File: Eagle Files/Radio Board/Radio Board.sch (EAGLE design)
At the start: 15 parts, among them Y1 16 MHZ

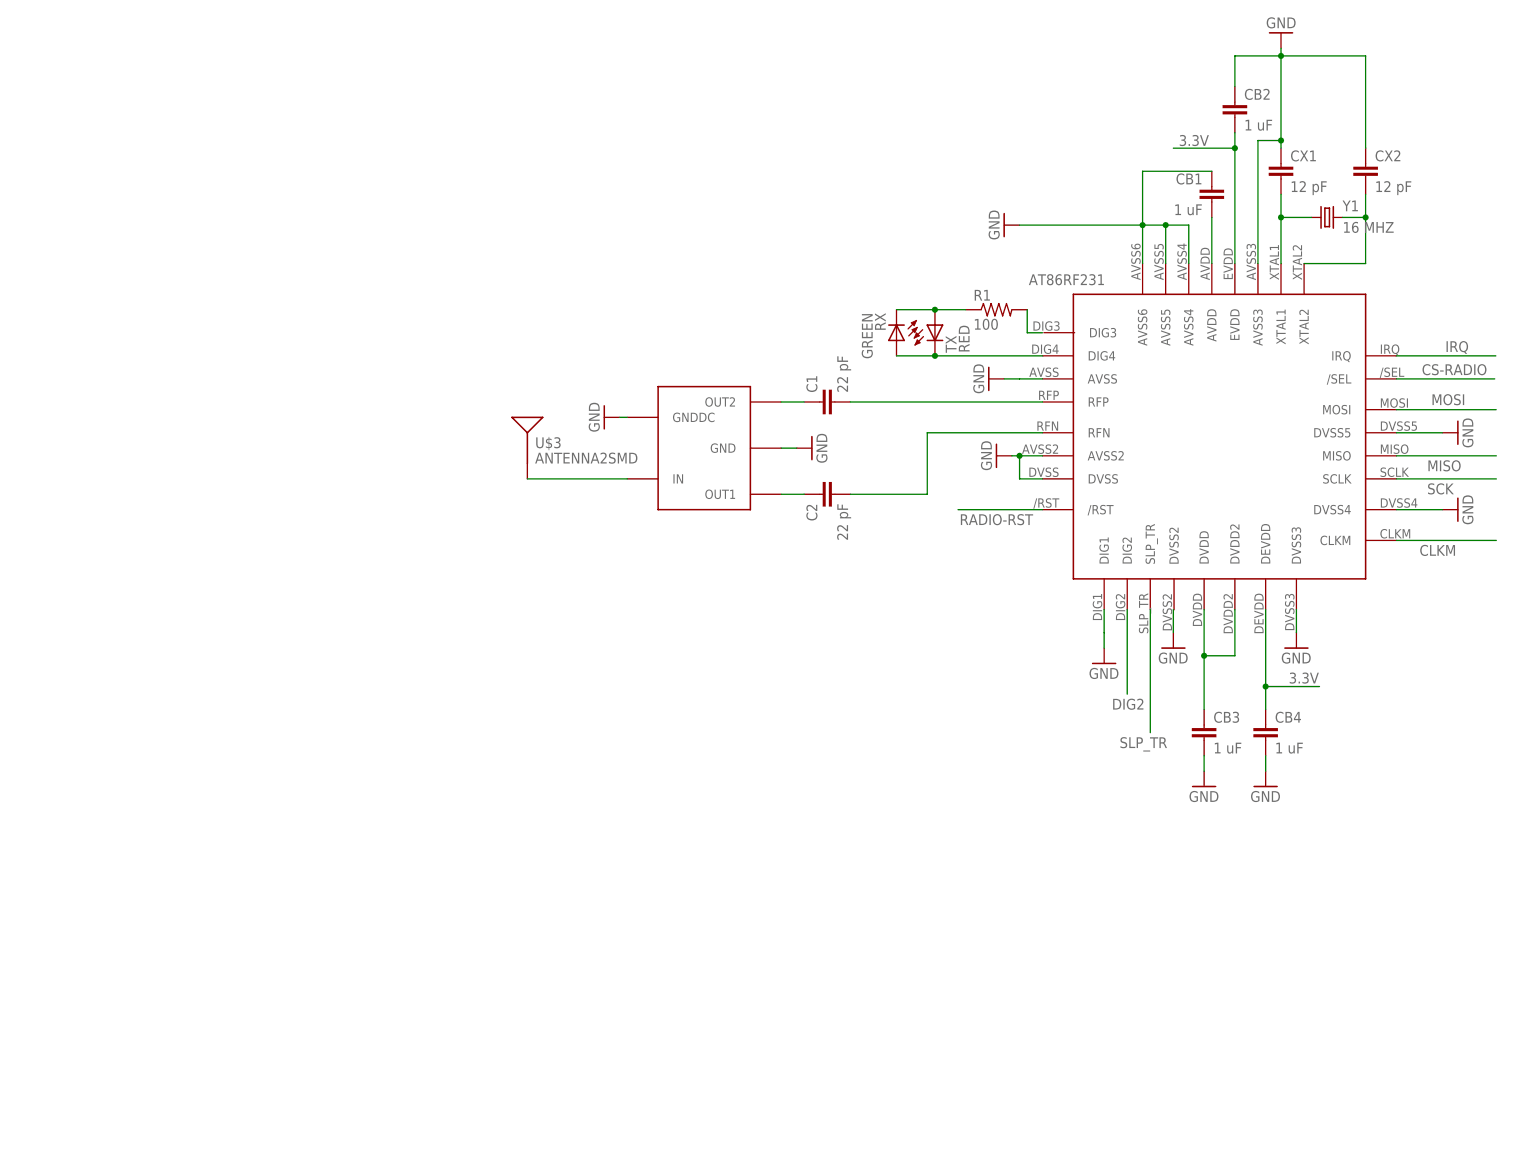
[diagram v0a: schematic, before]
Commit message: The Radio Board is now ready to be used with a 10 pin header.
--Arthur

git-svn-id: http://cd-net.net/CPE496/trunk@87 05b6d0e0-c345-4a8e-a5b7-579c8bd0b646
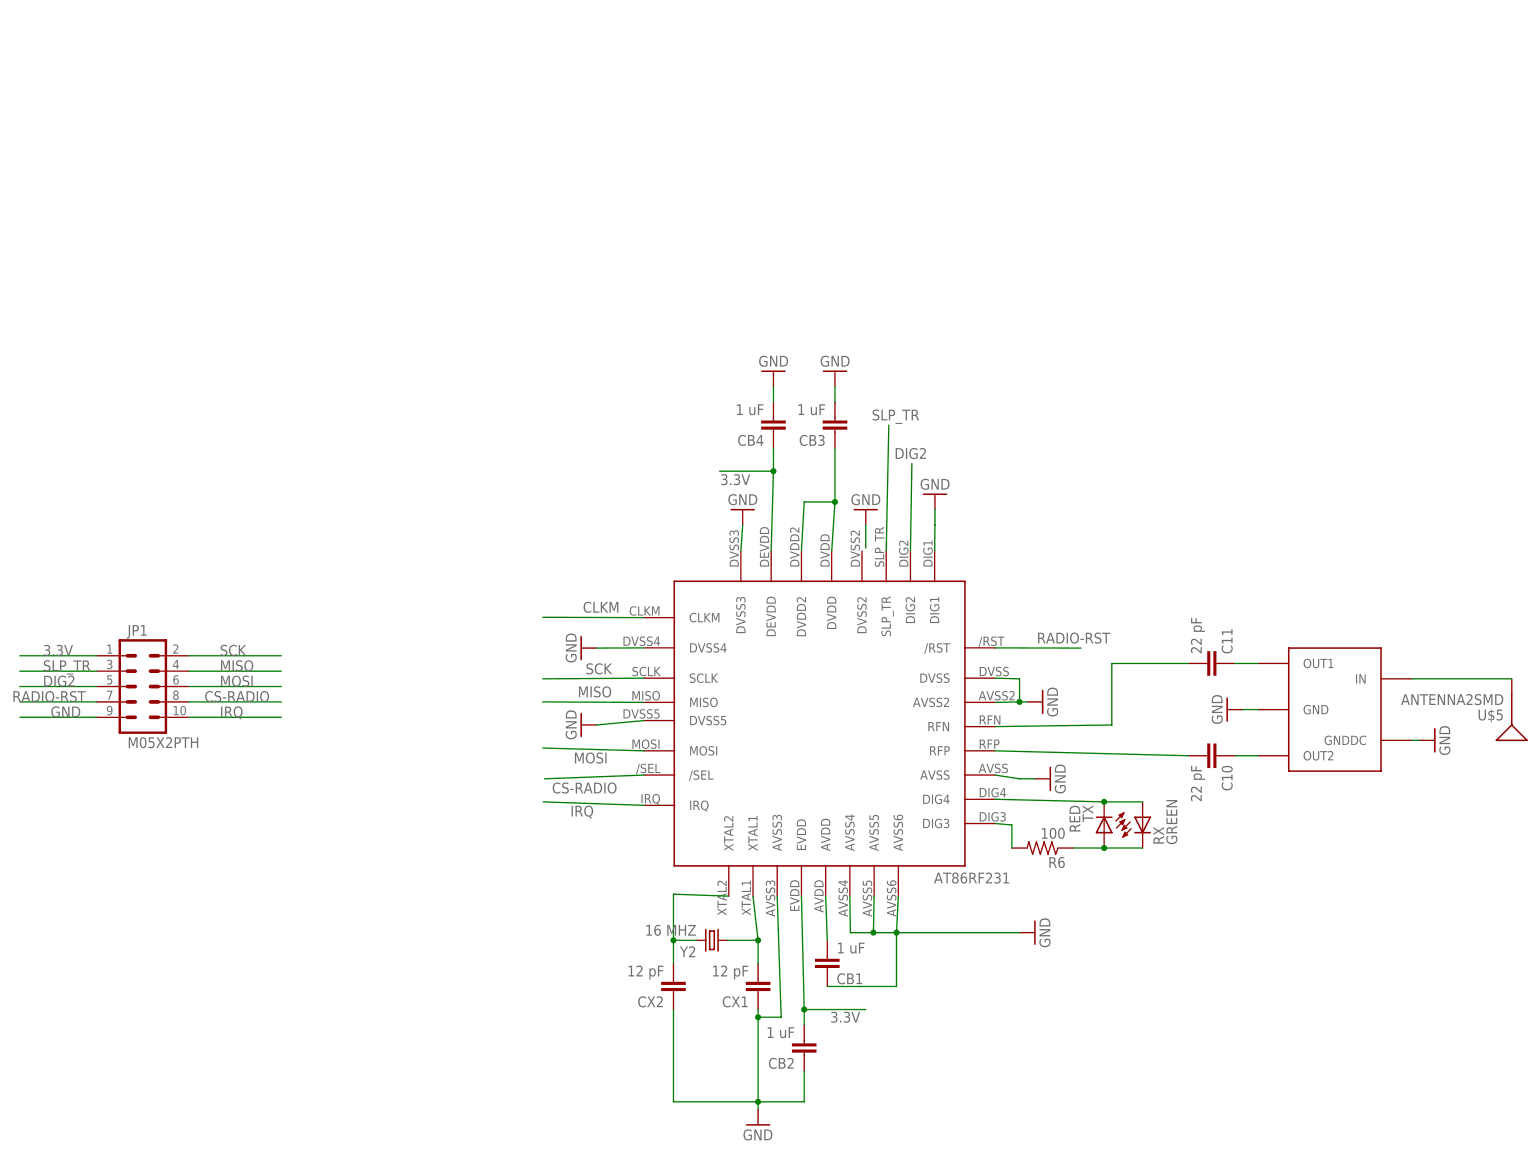
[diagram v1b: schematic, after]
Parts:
- removed C1, C2: 22 pF, SparkFun:CAP0603-CAP
- removed R1: 100, SparkFun:RESISTOR0603-RES
- removed U$1: AT86RF231(RADIO)AT86RF231, group10:AT86RF231(RADIO)AT86RF231
- removed U$2: WE-BAL, group10:WE-BAL
- removed Y1: 16 MHZ, group10:CRYSTALHC49US
- added C10, C11: 22 pF, SparkFun:CAP0603-CAP
- added JP1: M05X2PTH, SparkFun:M05X2PTH
- added R6: 100, SparkFun:RESISTOR0603-RES
- added U$4: WE-BAL, group10:WE-BAL
- added U$5: ANTENNA2SMD, SparkFun:ANTENNA2SMD
- added Y2: 16 MHZ, group10:CRYSTALSMD
- U$3: value ANTENNA2SMD -> AT86RF231(RADIO)AT86RF231; device SparkFun:ANTENNA2SMD -> group10:AT86RF231(RADIO)AT86RF231
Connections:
- removed net N$1: CB3.1, U$1.DVDD, U$1.DVDD2
- removed net N$2: CB1.2, U$1.AVDD
- removed net N$3: CX1.2, U$1.XTAL1, Y1.1
- removed net N$4: CX2.2, U$1.XTAL2, Y1.2
- removed net N$5: RX.A, TX.C, U$1.DIG4
- removed net N$6: R1.1, RX.C, TX.A
- removed net N$7: R1.2
- removed net N$8: C1.1, U$2.OUT2
- new net N$13: RX.A, TX.C, U$3.DIG4
- new net N$14: R6.1, RX.C, TX.A
- new net N$15: R6.2, U$3.DIG3
- new net N$16: C10.1, U$4.OUT2
- new net N$17: C11.1, U$4.OUT1
- new net N$18: C11.2, U$3.RFN
- new net N$19: C10.2, U$3.RFP
- new net N$20: U$4.IN, U$5.SIGNAL
- net 3.3V: now also JP1.1, U$3.DEVDD, U$3.EVDD; no longer U$1.DEVDD, U$1.EVDD
- net CLKM: now also U$3.CLKM; no longer U$1.CLKM
- net CS-RADIO: now also JP1.8, U$3./SEL; no longer U$1./SEL
- net DIG2: now also JP1.5, U$3.DIG2; no longer U$1.DIG2
- net GND: now also JP1.9, U$3.AVSS, U$3.AVSS2, U$3.AVSS3, U$3.AVSS4, U$3.AVSS5, U$3.AVSS6, U$3.DIG1, U$3.DVSS, U$3.DVSS3, U$3.DVSS4, U$3.DVSS5, U$4.GND, U$4.GNDDC; no longer U$1.AVSS, U$1.AVSS2, U$1.AVSS3, U$1.AVSS4, U$1.AVSS5, U$1.AVSS6, U$1.DIG1, U$1.DVSS, U$1.DVSS3, U$1.DVSS4, U$1.DVSS5, U$2.GND, U$2.GNDDC
- net IRQ: now also JP1.10, U$3.IRQ; no longer U$1.IRQ
- net MISO: now also JP1.4, U$3.MISO; no longer U$1.MISO
- net MOSI: now also JP1.6, U$3.MOSI; no longer U$1.MOSI
- net N$10: now also CB1.2, U$3.AVDD; no longer C1.2, U$1.RFP
- net N$11: now also CX1.2, U$3.XTAL1, Y2.1; no longer C2.2, U$1.RFN
- net N$12: now also CX2.2, U$3.XTAL2, Y2.2; no longer U$2.IN, U$3.SIGNAL
- net N$9: now also CB3.1, U$3.DVDD, U$3.DVDD2; no longer C2.1, U$2.OUT1
- net RADIO-RST: now also JP1.7, U$3./RST; no longer U$1./RST
- net SCK: now also JP1.2, U$3.SCLK; no longer U$1.SCLK
- net SLP_TR: now also JP1.3, U$3.SLP_TR; no longer U$1.SLP_TR
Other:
- moved on the sheet: CB1, CB2, CB3, CB4, CX1, CX2, RX, TX

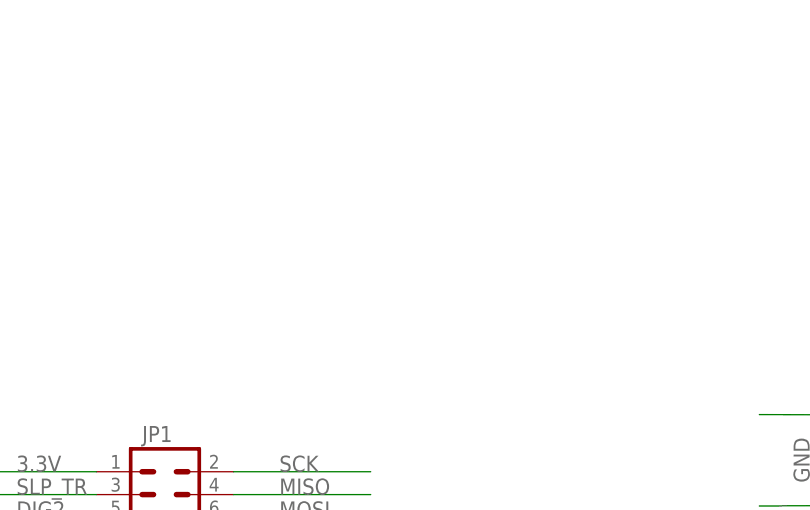
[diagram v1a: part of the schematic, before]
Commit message: Radio Board now has pull up resistors on Radio Reset, and Radio CS.
--Arthur

git-svn-id: http://cd-net.net/CPE496/trunk@90 05b6d0e0-c345-4a8e-a5b7-579c8bd0b646
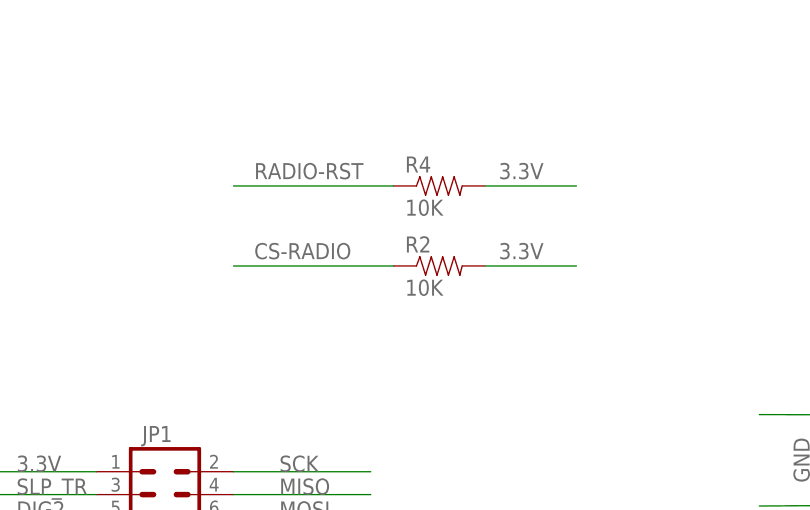
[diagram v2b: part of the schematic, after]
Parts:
- added R2, R4: 10K, SparkFun:RESISTOR0603-RES
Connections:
- net 3.3V: now also R2.2, R4.2
- net CS-RADIO: now also R2.1
- net RADIO-RST: now also R4.1
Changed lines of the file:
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@@
 <grid distance="0.1" unitdist="inch" unit="inch" style="lines" multiple="1" display="no" altdistance="0.01" altunitdist="inch" altunit="inch"/>
 <layers>
-<layer number="1" name="Top" color="4" fill="1" visible="yes" active="no"/>
-<layer number="16" name="Bottom" color="1" fill="1" visible="yes" active="no"/>
-<layer number="17" name="Pads" color="2" fill="1" visible="yes" active="no"/>
-<layer number="18" name="Vias" color="2" fill="1" visible="yes" active="no"/>
-<layer number="19" name="Unrouted" color="6" fill="1" visible="yes" active="no"/>
-<layer number="20" name="Dimension" color="15" fill="1" visible="yes" active="no"/>
-<layer number="21" name="tPlace" color="16" fill="1" visible="yes" active="no"/>
-<layer number="22" name="bPlace" color="14" fill="1" visible="yes" active="no"/>
-<layer number="23" name="tOrigins" color="15" fill="1" visible="yes" active="no"/>
-<layer number="24" name="bOrigins" color="15" fill="1" visible="yes" active="no"/>
-<layer number="25" name="tNames" color="7" fill="1" visible="yes" active="no"/>
-<layer number="26" name="bNames" color="7" fill="1" visible="yes" active="no"/>
-<layer number="27" name="tValues" color="7" fill="1" visible="yes" active="no"/>
-<layer number="28" name="bValues" color="7" fill="1" visible="yes" active="no"/>
+<layer number="1" name="Top" color="4" fill="1" visible="no" active="no"/>
+<layer number="16" name="Bottom" color="1" fill="1" visible="no" active="no"/>
+<layer number="17" name="Pads" color="2" fill="1" visible="no" active="no"/>
+<layer number="18" name="Vias" color="2" fill="1" visible="no" active="no"/>
+<layer number="19" name="Unrouted" color="6" fill="1" visible="no" active="no"/>
+<layer number="20" name="Dimension" color="15" fill="1" visible="no" active="no"/>
+<layer number="21" name="tPlace" color="16" fill="1" visible="no" active="no"/>
+<layer number="22" name="bPlace" color="14" fill="1" visible="no" active="no"/>
+<layer number="23" name="tOrigins" color="15" fill="1" visible="no" active="no"/>
+<layer number="24" name="bOrigins" color="15" fill="1" visible="no" active="no"/>
+<layer number="25" name="tNames" color="7" fill="1" visible="no" active="no"/>
+<layer number="26" name="bNames" color="7" fill="1" visible="no" active="no"/>
+<layer number="27" name="tValues" color="7" fill="1" visible="no" active="no"/>
+<layer number="28" name="bValues" color="7" fill="1" visible="no" active="no"/>
 <layer number="29" name="tStop" color="7" fill="3" visible="no" active="no"/>
 <layer number="30" name="bStop" color="7" fill="6" visible="no" active="no"/>
@@
 <layer number="35" name="tGlue" color="7" fill="4" visible="no" active="no"/>
 <layer number="36" name="bGlue" color="7" fill="5" visible="no" active="no"/>
-<layer number="37" name="tTest" color="7" fill="1" visible="yes" active="no"/>
-<layer number="38" name="bTest" color="7" fill="1" visible="yes" active="no"/>
+<layer number="37" name="tTest" color="7" fill="1" visible="no" active="no"/>
+<layer number="38" name="bTest" color="7" fill="1" visible="no" active="no"/>
 <layer number="39" name="tKeepout" color="4" fill="11" visible="no" active="no"/>
 <layer number="40" name="bKeepout" color="1" fill="11" visible="no" active="no"/>
@@
 <layer number="44" name="Drills" color="7" fill="1" visible="no" active="no"/>
 <layer number="45" name="Holes" color="7" fill="1" visible="no" active="no"/>
-<layer number="46" name="Milling" color="3" fill="1" visible="yes" active="no"/>
-<layer number="47" name="Measures" color="7" fill="1" visible="yes" active="no"/>
-<layer number="48" name="Document" color="7" fill="1" visible="yes" active="no"/>
-<layer number="49" name="Reference" color="7" fill="1" visible="yes" active="no"/>
-<layer number="50" name="dxf" color="7" fill="1" visible="yes" active="no"/>
-<layer number="51" name="tDocu" color="6" fill="1" visible="yes" active="no"/>
-<layer number="52" name="bDocu" color="7" fill="1" visible="yes" active="no"/>
-<layer number="53" name="tGND_GNDA" color="7" fill="9" visible="yes" active="no"/>
-<layer number="54" name="bGND_GNDA" color="1" fill="9" visible="yes" active="no"/>
-<layer number="56" name="wert" color="7" fill="1" visible="yes" active="no"/>
+<layer number="46" name="Milling" color="3" fill="1" visible="no" active="no"/>
+<layer number="47" name="Measures" color="7" fill="1" visible="no" active="no"/>
+<layer number="48" name="Document" color="7" fill="1" visible="no" active="no"/>
+<layer number="49" name="Reference" color="7" fill="1" visible="no" active="no"/>
+<layer number="50" name="dxf" color="7" fill="1" visible="no" active="no"/>
+<layer number="51" name="tDocu" color="6" fill="1" visible="no" active="no"/>
+<layer number="52" name="bDocu" color="7" fill="1" visible="no" active="no"/>
+<layer number="53" name="tGND_GNDA" color="7" fill="9" visible="no" active="no"/>
+<layer number="54" name="bGND_GNDA" color="1" fill="9" visible="no" active="no"/>
+<layer number="56" name="wert" color="7" fill="1" visible="no" active="no"/>
 <layer number="91" name="Nets" color="2" fill="1" visible="yes" active="yes"/>
 <layer number="92" name="Busses" color="1" fill="1" visible="yes" active="yes"/>
@@
 <part name="U$5" library="SparkFun" deviceset="ANTENNA2" device="SMD"/>
 <part name="JP1" library="SparkFun" deviceset="M05X2" device="PTH"/>
+<part name="R2" library="SparkFun" deviceset="RESISTOR" device="0603-RES" value="10K"/>
+<part name="R4" library="SparkFun" deviceset="RESISTOR" device="0603-RES" value="10K"/>
 </parts>
 <sheets>
@@
 <instance part="U$5" gate="G$1" x="114.3" y="3.81" rot="R180"/>
 <instance part="JP1" gate="G$1" x="-111.76" y="7.62"/>
+<instance part="R2" gate="G$1" x="-81.28" y="35.56"/>
+<instance part="R4" gate="G$1" x="-81.28" y="44.45"/>
 </instances>
 <busses>
@@
 <label x="-128.27" y="12.7" size="1.778" layer="95"/>
 </segment>
+<segment>
+<pinref part="R2" gate="G$1" pin="2"/>
+<wire x1="-76.2" y1="35.56" x2="-66.04" y2="35.56" width="0.1524" layer="91"/>
+<label x="-74.676" y="36.322" size="1.778" layer="95"/>
+</segment>
+<segment>
+<pinref part="R4" gate="G$1" pin="2"/>
+<wire x1="-76.2" y1="44.45" x2="-66.04" y2="44.45" width="0.1524" layer="91"/>
+<label x="-74.676" y="45.212" size="1.778" layer="95"/>
+</segment>
 </net>
 <net name="SCK" class="0">
@@
 <label x="-101.6" y="5.08" size="1.778" layer="95"/>
 </segment>
+<segment>
+<pinref part="R2" gate="G$1" pin="1"/>
+<wire x1="-86.36" y1="35.56" x2="-104.14" y2="35.56" width="0.1524" layer="91"/>
+<label x="-101.854" y="36.322" size="1.778" layer="95"/>
+</segment>
 </net>
 <net name="RADIO-RST" class="0">
@@
 <label x="-133.35" y="5.08" size="1.778" layer="95"/>
 </segment>
-</net>
+<segment>
+<pinref part="R4" gate="G$1" pin="1"/>
+<wire x1="-86.36" y1="44.45" x2="-104.14" y2="44.45" width="0.1524" layer="91"/>
+<label x="-101.854" y="45.212" size="1.778" layer="95"/>
+</segment>
+</net>

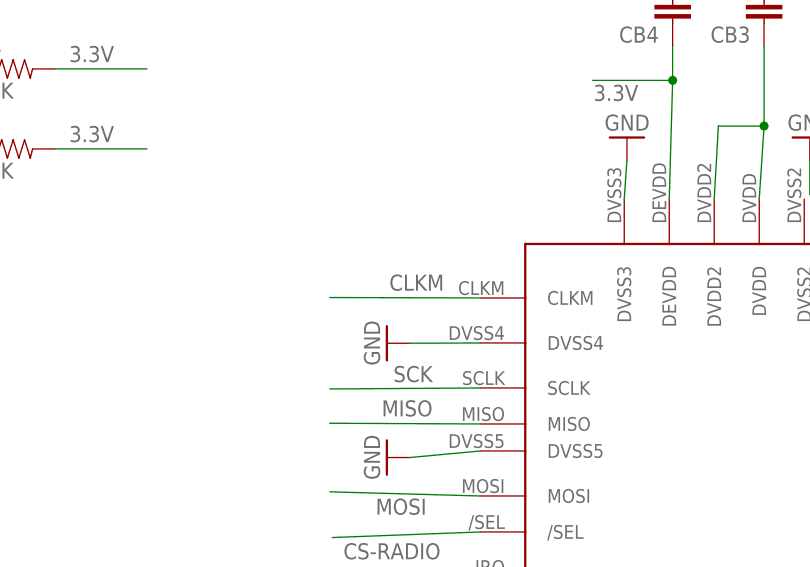
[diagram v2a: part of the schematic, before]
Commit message: Main Board with Headers is now almost ready.
I'm adding the FTDI Module right now.

TODO:
1.  Double check regulator Datasheet.  I think we're missing a capacitor.
2.  Update Radio Module Schematics to incorporate ground plane.
3.  Check if the hall effect sensor can work linearly at 3.3V
4.  Finish Adding FTDI chip and USB connector.

--Arthur

git-svn-id: http://cd-net.net/CPE496/trunk@119 05b6d0e0-c345-4a8e-a5b7-579c8bd0b646
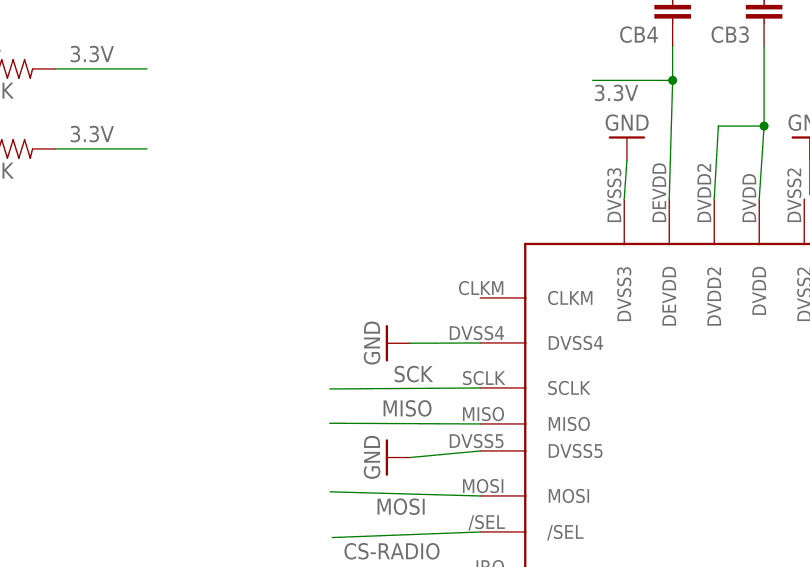
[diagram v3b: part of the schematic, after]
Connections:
- removed net CLKM: U$3.CLKM
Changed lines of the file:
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@@
-</segment>
-</net>
-<net name="CLKM" class="0">
-<segment>
-<pinref part="U$3" gate="G$1" pin="CLKM"/>
-<wire x1="-29" y1="19" x2="-45.72" y2="19.05" width="0.1524" layer="91"/>
-<label x="-33.02" y="21.59" size="1.778" layer="95" rot="R180"/>
 </segment>
 </net>
